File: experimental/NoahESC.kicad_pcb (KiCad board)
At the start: 2 copper layers, 90 x 39.1 mm, 48 parts, among them J1 5V, J10 GND, J12 PWM_IN, J2 12V, J3 GND, J7 DTR, J8 TX, J9 RX, Q1 IRLR7843TRPBF, Q2 IRLR7843TRPBF, Q3 IRLR7843TRPBF, Q4 IRLR7843TRPBF, Q5 IRLR7843TRPBF, Q6 IRLR7843TRPBF, U1 IR2101, U2 IR2101, U3 IR2101, U4 L7805, U5 ATmega328, Y1 16Mhz

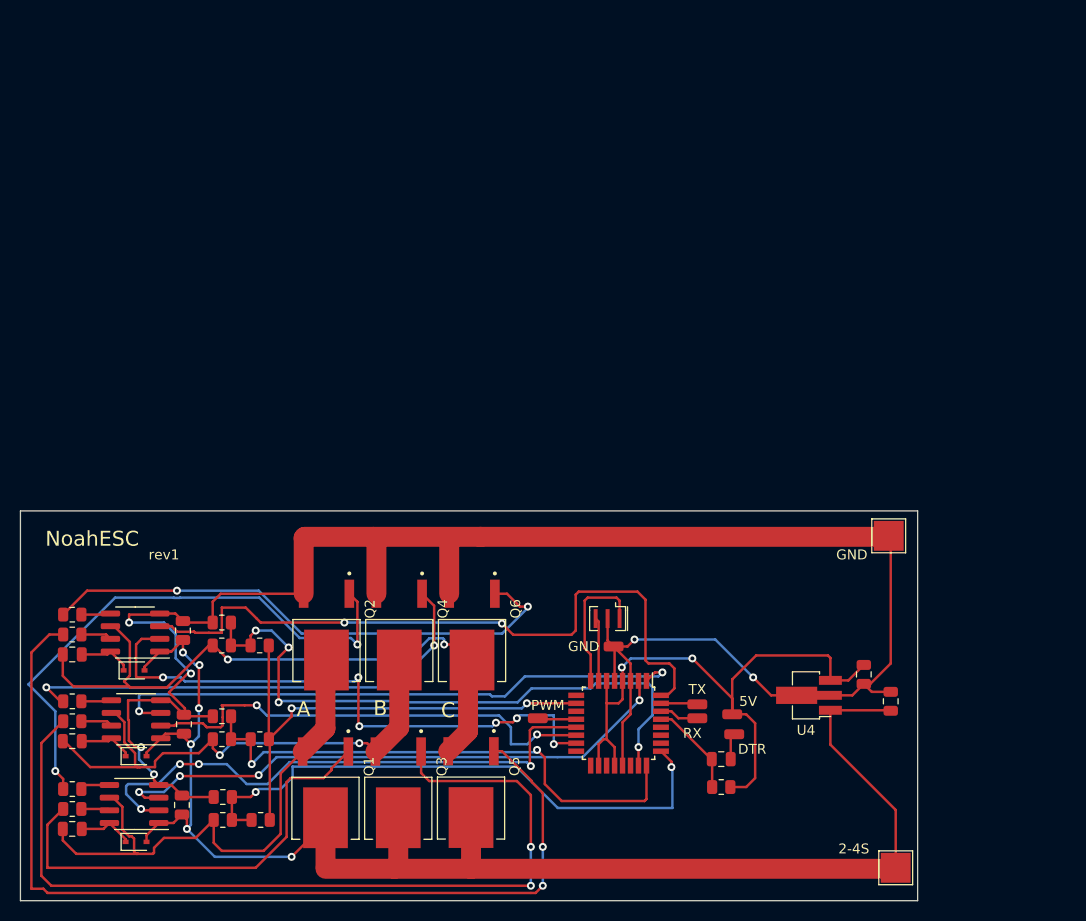
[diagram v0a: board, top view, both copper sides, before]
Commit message: DIP version
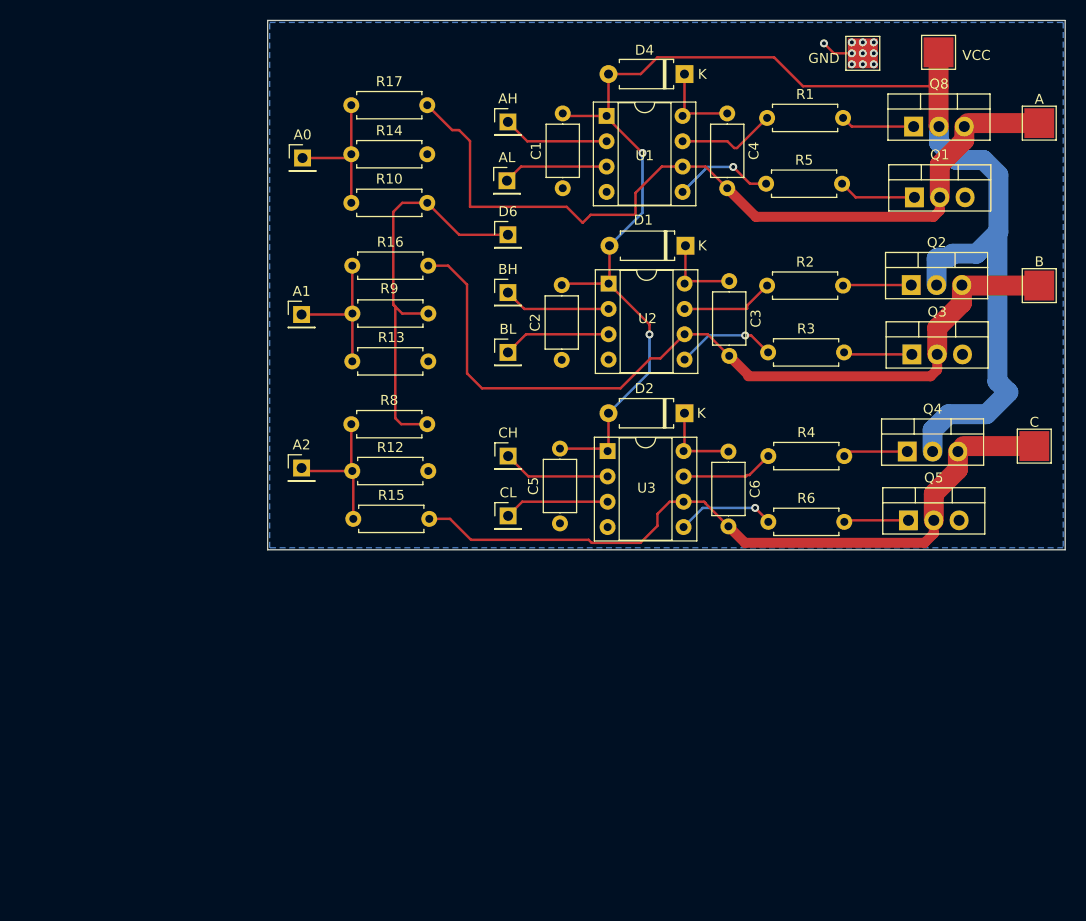
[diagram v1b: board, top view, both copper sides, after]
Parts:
- removed C17: 1nF, Capacitor_SMD:C_0805_2012Metric
- removed C7: 330nF, Capacitor_SMD:C_0805_2012Metric
- removed C8: 100nF, Capacitor_SMD:C_0805_2012Metric
- removed D3: 1N4148WS, Diode_SMD:D_SOD-323
- removed J1: 5V, Connector_Wire:SolderWirePad_1x01_SMD_1x2mm
- removed J10: GND, Connector_Wire:SolderWirePad_1x01_SMD_1x2mm
- removed J12: PWM_IN, Connector_Wire:SolderWirePad_1x01_SMD_1x2mm
- removed J2: 12V, TestPoint:TestPoint_Pad_3.0x3.0mm
- removed J3: GND, TestPoint:TestPoint_Pad_3.0x3.0mm
- removed J7: DTR, Connector_Wire:SolderWirePad_1x01_SMD_1x2mm
- removed J8: TX, Connector_Wire:SolderWirePad_1x01_SMD_1x2mm
- removed J9: RX, Connector_Wire:SolderWirePad_1x01_SMD_1x2mm
- removed Q6: IRLR7843TRPBF, IRLR7843TRPBF:TO229P990X239-3_4N
- removed R20: 10K, Resistor_SMD:R_0805_2012Metric
- removed U4: L7805, Package_TO_SOT_SMD:SOT-89-3_Handsoldering
- removed U5: ATmega328, Package_QFP:TQFP-32_7x7mm_P0.8mm
- removed Y1: 16Mhz, Crystal:Resonator_SMD_Murata_CSTxExxV-3Pin_3.0x1.1mm
- added A: PHASE_A, TestPoint:TestPoint_Pad_3.0x3.0mm, F.Cu at (186.3, 71.0)
- added A0: A0, Connector_PinHeader_2.54mm:PinHeader_1x01_P2.54mm_Vertical, F.Cu at (112.4, 74.5)
- added A1: A1, Connector_PinHeader_2.54mm:PinHeader_1x01_P2.54mm_Vertical, F.Cu at (112.3, 90.2)
- added A2: A2, Connector_PinHeader_2.54mm:PinHeader_1x01_P2.54mm_Vertical, F.Cu at (112.3, 105.6)
- added AH: AH, Connector_PinHeader_2.54mm:PinHeader_1x01_P2.54mm_Vertical, F.Cu at (133.0, 70.9)
- added AL: AL, Connector_PinHeader_2.54mm:PinHeader_1x01_P2.54mm_Vertical, F.Cu at (132.9, 76.8)
- added B: PHASE_B, TestPoint:TestPoint_Pad_3.0x3.0mm, F.Cu at (186.3, 87.3)
- added BH: BH, Connector_PinHeader_2.54mm:PinHeader_1x01_P2.54mm_Vertical, F.Cu at (133.0, 88.0)
- added BL: BL, Connector_PinHeader_2.54mm:PinHeader_1x01_P2.54mm_Vertical, F.Cu at (133.0, 94.0)
- added C: PHASE_C, TestPoint:TestPoint_Pad_3.0x3.0mm, F.Cu at (185.8, 103.4)
- added CH: CH, Connector_PinHeader_2.54mm:PinHeader_1x01_P2.54mm_Vertical, F.Cu at (133.0, 104.4)
- added CL: CL, Connector_PinHeader_2.54mm:PinHeader_1x01_P2.54mm_Vertical, F.Cu at (133.0, 110.4)
- added D4: D, Diode_THT:D_A-405_P7.62mm_Horizontal, F.Cu at (150.7, 66.1)
- added D6: D6, Connector_PinHeader_2.54mm:PinHeader_1x01_P2.54mm_Vertical, F.Cu at (133.0, 82.2)
- added GND: GND, TestPoint:TestPoint_Pad_3.0x3.0mm, F.Cu at (168.6, 64.0)
- added Q8: NMOS, Package_TO_SOT_THT:TO-220-3_Vertical, F.Cu at (173.7, 71.3)
- added VCC: 12V, TestPoint:TestPoint_Pad_3.0x3.0mm, F.Cu at (176.2, 63.9)
- C1, C2, C4, C6: footprint Capacitor_SMD:C_0805_2012Metric -> Capacitor_THT:C_Axial_L5.1mm_D3.1mm_P7.50mm_Horizontal
- C3: value 10uF -> 2.2uF; footprint Capacitor_SMD:C_0805_2012Metric -> Capacitor_THT:C_Axial_L5.1mm_D3.1mm_P7.50mm_Horizontal
- C5: value 2.2uF -> 10uF; footprint Capacitor_SMD:C_0805_2012Metric -> Capacitor_THT:C_Axial_L5.1mm_D3.1mm_P7.50mm_Horizontal
- D1, D2: value 1N4148WS -> D; footprint Diode_SMD:D_SOD-323 -> Diode_THT:D_A-405_P7.62mm_Horizontal
- Q1, Q2, Q3, Q4, Q5: value IRLR7843TRPBF -> NMOS; footprint IRLR7843TRPBF:TO229P990X239-3_4N -> Package_TO_SOT_THT:TO-220-3_Vertical
- R1, R10, R12, R13, R14, R15, R16, R17, R2, R3, R4, R5, R6, R8, R9: footprint Resistor_SMD:R_0805_2012Metric -> Resistor_THT:R_Axial_DIN0207_L6.3mm_D2.5mm_P7.62mm_Horizontal
- U1, U2, U3: footprint Package_SO:SOIC-8_3.9x4.9mm_P1.27mm -> Package_DIP:DIP-8_W7.62mm_Socket
- moved R1 98.3 mm to (159.0, 70.5), turned to 0 degrees
- moved C4 97.3 mm to (155.0, 70.0), turned to -90 degrees
- moved R5 92.4 mm to (158.9, 77.1), turned to 0 degrees
- moved Q1 85.8 mm to (173.8, 78.4), turned to 0 degrees
- moved U1 83.7 mm to (142.9, 70.3), turned to 0 degrees
- moved D1 81.3 mm to (150.8, 83.3), turned to 180 degrees
- moved R3 79.0 mm to (159.1, 94.0), turned to 0 degrees
- moved R2 78.0 mm to (159.0, 87.3), turned to 0 degrees
- moved R4 74.0 mm to (159.1, 104.4), turned to 0 degrees
- moved C1 72.7 mm to (138.5, 77.5), turned to 90 degrees
- moved R6 70.4 mm to (159.1, 111.0), turned to 0 degrees
- moved Q2 69.7 mm to (173.5, 87.2), turned to 0 degrees
- moved Q3 69.4 mm to (173.5, 94.2), turned to 0 degrees
- moved C6 68.9 mm to (155.1, 104.0), turned to -90 degrees
- moved C3 65.1 mm to (155.2, 86.8)
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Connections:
- C3 pad 1: GND -> Net-(D1-K)
- C3 pad 2: 12V -> PHASE_B
- C4 pad 1: Net-(C4-Pad1) -> Net-(D4-K)
- C5 pad 1: Net-(C5-Pad1) -> GND
- C5 pad 2: PHASE_B -> 12V
- C6 pad 1: Net-(C6-Pad1) -> Net-(D2-K)
- D1 pad 1: Net-(C4-Pad1) -> Net-(D1-K)
- D2 pad 1: Net-(C5-Pad1) -> Net-(D2-K)
- Q1 pad 1: Net-(Q1-Pad1) -> Net-(Q1-G)
- Q1 pad 3: PHASE_A -> GND
- Q2 pad 1: Net-(Q2-Pad1) -> Net-(Q2-G)
- Q2 pad 3: GND -> PHASE_B
- Q3 pad 3: PHASE_B -> GND
- Q4 pad 3: GND -> PHASE_C
- Q5 pad 1: Net-(Q5-Pad1) -> Net-(Q5-G)
- Q5 pad 3: PHASE_C -> GND
- R1 pad 2: Net-(Q1-Pad1) -> Net-(Q8-G)
- R15 pad 2: PHASE_A -> PHASE_C
- R17 pad 2: PHASE_C -> PHASE_A
- R2 pad 1: Net-(R2-Pad1) -> Net-(U2-HO)
- R2 pad 2: Net-(Q5-Pad1) -> Net-(Q2-G)
- R3 pad 1: Net-(R3-Pad1) -> Net-(U2-LO)
- R4 pad 1: Net-(R4-Pad1) -> Net-(U3-HO)
- R5 pad 2: Net-(Q2-Pad1) -> Net-(Q1-G)
- R6 pad 2: Net-(Q6-Pad1) -> Net-(Q5-G)
- U1 pad 8: Net-(C4-Pad1) -> Net-(D4-K)
- U2 pad 5: Net-(R4-Pad1) -> Net-(U2-LO)
- U2 pad 7: Net-(R3-Pad1) -> Net-(U2-HO)
- U2 pad 8: Net-(C5-Pad1) -> Net-(D1-K)
- U3 pad 7: Net-(R2-Pad1) -> Net-(U3-HO)
- U3 pad 8: Net-(C6-Pad1) -> Net-(D2-K)
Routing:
- net GND: track 205.6 -> 4.31 mm, vias 6 -> 10
- net Net-(Q5-Pad1): track 95.4 -> 0.00 mm, vias 2 -> 0
- net Net-(Q3-G): track 89.1 -> 6.88 mm, vias 2 -> 0
- net 5V: track 63.3 -> 0.00 mm, vias 2 -> 0
- net CL: track 69.9 -> 10.6 mm, vias 2 -> 0
- net Net-(Q2-Pad1): track 55.9 -> 0.00 mm, vias 2 -> 0
- net Net-(Q6-Pad1): track 54.4 -> 0.00 mm, vias 2 -> 0
- net BL: track 59.4 -> 10.9 mm, vias 2 -> 0
- net A0: track 62.9 -> 14.8 mm, vias 4 -> 0
- net CH: track 58.6 -> 10.8 mm, vias 6 -> 0
- net AL: track 58.2 -> 10.6 mm, vias 4 -> 0
- net AH: track 56.6 -> 10.7 mm, vias 4 -> 0
- net Net-(Q1-Pad1): track 44.9 -> 0.00 mm
- net A2: track 58.2 -> 14.8 mm, vias 2 -> 0
- net Net-(Q4-G): track 48.6 -> 6.51 mm, vias 2 -> 0
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- added copper zone on B.Cu, net GND
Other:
- board size 90 x 39.1 mm -> 80 x 53.1 mm
- board text removed: "2-4S"
- board text removed: "5V"
- board text removed: "A"
- board text removed: "B"
- board text removed: "C"
- board text removed: "DTR"
- board text removed: "GND"
- board text removed: "NoahESC"
- board text removed: "PWM"
- board text removed: "RX"
- board text removed: "TX"
- board text removed: "https://github.com/zosko/NoahESC by Bosko"
- board text removed: "rev1"
